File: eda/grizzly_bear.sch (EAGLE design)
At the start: 60 parts, among them Q1 N-CHANNEL-MOSFET, Q2 N-CHANNEL-MOSFET, Q3 N-CHANNEL-MOSFET, Q4 N-CHANNEL-MOSFET, Q5 IPD90P03P4L, U1 A4940, U2 ATMEGA32U4-AU, U3 ACS714, U4 UA78L00, U5 ISL83491SOIC, Y1 16MHz

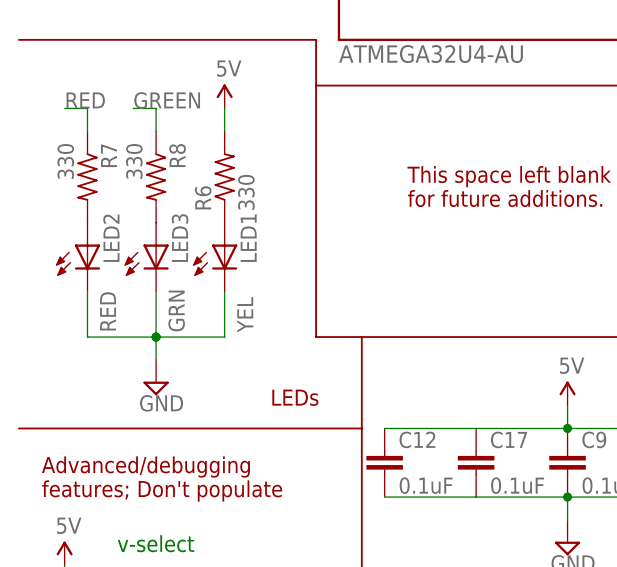
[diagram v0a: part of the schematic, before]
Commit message: Fix some LED BOM values
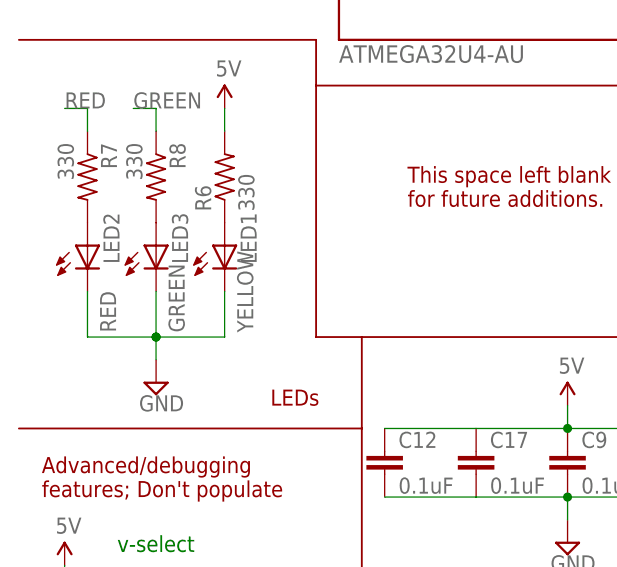
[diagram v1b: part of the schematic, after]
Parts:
- LED1: value YEL -> YELLOW
- LED3: value GRN -> GREEN
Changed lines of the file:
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@@
 <part name="C9" library="pie" deviceset="CAP" device="0603-CAP" value="0.1uF"/>
 <part name="LED2" library="pie" deviceset="LED" device="0805" value="RED"/>
-<part name="LED3" library="pie" deviceset="LED" device="0805" value="GRN"/>
+<part name="LED3" library="pie" deviceset="LED" device="0805" value="GREEN"/>
 <part name="R8" library="pie" deviceset="R-US_" device="R0603" value="330"/>
 <part name="R7" library="pie" deviceset="R-US_" device="R0603" value="330"/>
-<part name="LED1" library="pie" deviceset="LED" device="0805" value="YEL"/>
+<part name="LED1" library="pie" deviceset="LED" device="0805" value="YELLOW"/>
 <part name="R6" library="pie" deviceset="R-US_" device="R0603" value="330"/>
 <part name="U$13" library="pie" deviceset="5V" device=""/>

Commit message: Add even more BOM metadata
Only missing a small handful of parts
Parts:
- C8: value 470nF -> .47 uF
- Q1, Q2, Q3, Q4: value N-CHANNEL-MOSFET -> PSMN4R0
- SV2: device con-lstb:MA04-2 -> pie:MA04-2
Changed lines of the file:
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@@
 <part name="U$5" library="pie" deviceset="5V" device=""/>
 <part name="C16" library="pie" deviceset="CAP" device="0603-CAP" value="0.1uF"/>
-<part name="C8" library="pie" deviceset="CAP" device="0603-CAP" value="470nF"/>
+<part name="C8" library="pie" deviceset="CAP" device="0603-CAP" value=".47 uF"/>
 <part name="C6" library="pie" deviceset="CAP" device="0603-CAP" value="1uF"/>
 <part name="C7" library="pie" deviceset="CAP" device="0603-CAP" value="33nF"/>
@@
 <part name="Y1" library="pie" deviceset="CRYSTAL" device="SMD" value="16MHz"/>
 <part name="SV1" library="pie" deviceset="MA03-2" device=""/>
-<part name="Q1" library="pie" deviceset="N-CHANNEL-MOSFET" device=""/>
-<part name="Q2" library="pie" deviceset="N-CHANNEL-MOSFET" device=""/>
-<part name="Q3" library="pie" deviceset="N-CHANNEL-MOSFET" device=""/>
-<part name="Q4" library="pie" deviceset="N-CHANNEL-MOSFET" device=""/>
+<part name="Q1" library="pie" deviceset="N-CHANNEL-MOSFET" device="" value="PSMN4R0"/>
+<part name="Q2" library="pie" deviceset="N-CHANNEL-MOSFET" device="" value="PSMN4R0"/>
+<part name="Q3" library="pie" deviceset="N-CHANNEL-MOSFET" device="" value="PSMN4R0"/>
+<part name="Q4" library="pie" deviceset="N-CHANNEL-MOSFET" device="" value="PSMN4R0"/>
 <part name="Q5" library="pie" deviceset="P-CHANNEL-MOSFET" device="TO252" value="IPD90P03P4L"/>
 <part name="JP1" library="pie" deviceset="M02" device="PTH" value="GND"/>
@@
 <part name="SUPPLY9" library="pie" deviceset="GND" device=""/>
 <part name="U$15" library="pie" deviceset="5V" device=""/>
-<part name="SV2" library="con-lstb" deviceset="MA04-2" device=""/>
+<part name="SV2" library="pie" deviceset="MA04-2" device=""/>
 <part name="C17" library="pie" deviceset="CAP" device="0603-CAP" value="0.1uF"/>
 </parts>

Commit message: All BOM metadata for explicit parts added
Changed C4 on Grizzly to 1206 and moved around parts so that plane
is not interrupted as much.

Smartsensor filter permutations are not embedded in the BOM metadata
and will be documented elsewhere.
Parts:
- C4: device pie:CAP0603-CAP -> pie:CAP1206
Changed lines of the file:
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@@
 <grid distance="0.1" unitdist="inch" unit="inch" style="lines" multiple="1" display="yes" altdistance="0.05" altunitdist="inch" altunit="inch"/>
 <layers>
-<layer number="1" name="Top" color="4" fill="1" visible="no" active="no"/>
-<layer number="2" name="Route2" color="1" fill="3" visible="no" active="no"/>
-<layer number="3" name="Route3" color="4" fill="3" visible="no" active="no"/>
-<layer number="4" name="Route4" color="1" fill="4" visible="no" active="no"/>
-<layer number="5" name="Route5" color="4" fill="4" visible="no" active="no"/>
-<layer number="6" name="Route6" color="1" fill="8" visible="no" active="no"/>
-<layer number="7" name="Route7" color="4" fill="8" visible="no" active="no"/>
-<layer number="8" name="Route8" color="1" fill="2" visible="no" active="no"/>
-<layer number="9" name="Route9" color="4" fill="2" visible="no" active="no"/>
-<layer number="10" name="Route10" color="1" fill="7" visible="no" active="no"/>
-<layer number="11" name="Route11" color="4" fill="7" visible="no" active="no"/>
-<layer number="12" name="Route12" color="1" fill="5" visible="no" active="no"/>
-<layer number="13" name="Route13" color="4" fill="5" visible="no" active="no"/>
-<layer number="14" name="Route14" color="1" fill="6" visible="no" active="no"/>
-<layer number="15" name="Route15" color="4" fill="6" visible="no" active="no"/>
-<layer number="16" name="Bottom" color="1" fill="1" visible="no" active="no"/>
-<layer number="17" name="Pads" color="2" fill="1" visible="no" active="no"/>
-<layer number="18" name="Vias" color="2" fill="1" visible="no" active="no"/>
-<layer number="19" name="Unrouted" color="6" fill="1" visible="no" active="no"/>
-<layer number="20" name="Dimension" color="15" fill="1" visible="no" active="no"/>
-<layer number="21" name="tPlace" color="16" fill="1" visible="no" active="no"/>
-<layer number="22" name="bPlace" color="14" fill="1" visible="no" active="no"/>
-<layer number="23" name="tOrigins" color="15" fill="1" visible="no" active="no"/>
-<layer number="24" name="bOrigins" color="15" fill="1" visible="no" active="no"/>
-<layer number="25" name="tNames" color="7" fill="1" visible="no" active="no"/>
-<layer number="26" name="bNames" color="12" fill="1" visible="no" active="no"/>
-<layer number="27" name="tValues" color="7" fill="1" visible="no" active="no"/>
-<layer number="28" name="bValues" color="12" fill="1" visible="no" active="no"/>
+<layer number="1" name="Top" color="4" fill="1" visible="yes" active="no"/>
+<layer number="2" name="Route2" color="1" fill="3" visible="yes" active="no"/>
+<layer number="3" name="Route3" color="20" fill="3" visible="yes" active="no"/>
+<layer number="4" name="Route4" color="21" fill="4" visible="yes" active="no"/>
+<layer number="5" name="Route5" color="4" fill="4" visible="yes" active="no"/>
+<layer number="6" name="Route6" color="1" fill="8" visible="yes" active="no"/>
+<layer number="7" name="Route7" color="4" fill="8" visible="yes" active="no"/>
+<layer number="8" name="Route8" color="1" fill="2" visible="yes" active="no"/>
+<layer number="9" name="Route9" color="4" fill="2" visible="yes" active="no"/>
+<layer number="10" name="Route10" color="1" fill="7" visible="yes" active="no"/>
+<layer number="11" name="Route11" color="4" fill="7" visible="yes" active="no"/>
+<layer number="12" name="Route12" color="1" fill="5" visible="yes" active="no"/>
+<layer number="13" name="Route13" color="4" fill="5" visible="yes" active="no"/>
+<layer number="14" name="Route14" color="1" fill="6" visible="yes" active="no"/>
+<layer number="15" name="Route15" color="4" fill="6" visible="yes" active="no"/>
+<layer number="16" name="Bottom" color="1" fill="1" visible="yes" active="no"/>
+<layer number="17" name="Pads" color="2" fill="1" visible="yes" active="no"/>
+<layer number="18" name="Vias" color="2" fill="1" visible="yes" active="no"/>
+<layer number="19" name="Unrouted" color="6" fill="1" visible="yes" active="no"/>
+<layer number="20" name="Dimension" color="15" fill="1" visible="yes" active="no"/>
+<layer number="21" name="tPlace" color="16" fill="1" visible="yes" active="no"/>
+<layer number="22" name="bPlace" color="17" fill="1" visible="yes" active="no"/>
+<layer number="23" name="tOrigins" color="15" fill="1" visible="yes" active="no"/>
+<layer number="24" name="bOrigins" color="15" fill="1" visible="yes" active="no"/>
+<layer number="25" name="tNames" color="18" fill="1" visible="yes" active="no"/>
+<layer number="26" name="bNames" color="19" fill="1" visible="yes" active="no"/>
+<layer number="27" name="tValues" color="18" fill="1" visible="yes" active="no"/>
+<layer number="28" name="bValues" color="19" fill="1" visible="yes" active="no"/>
 <layer number="29" name="tStop" color="7" fill="3" visible="no" active="no"/>
 <layer number="30" name="bStop" color="7" fill="6" visible="no" active="no"/>
@@
 <layer number="35" name="tGlue" color="7" fill="4" visible="no" active="no"/>
 <layer number="36" name="bGlue" color="7" fill="5" visible="no" active="no"/>
-<layer number="37" name="tTest" color="7" fill="1" visible="no" active="no"/>
-<layer number="38" name="bTest" color="7" fill="1" visible="no" active="no"/>
+<layer number="37" name="tTest" color="7" fill="1" visible="yes" active="no"/>
+<layer number="38" name="bTest" color="7" fill="1" visible="yes" active="no"/>
 <layer number="39" name="tKeepout" color="4" fill="11" visible="no" active="no"/>
 <layer number="40" name="bKeepout" color="1" fill="11" visible="no" active="no"/>
@@
 <layer number="44" name="Drills" color="7" fill="1" visible="no" active="no"/>
 <layer number="45" name="Holes" color="7" fill="1" visible="no" active="no"/>
-<layer number="46" name="Milling" color="3" fill="1" visible="no" active="no"/>
-<layer number="47" name="Measures" color="7" fill="1" visible="no" active="no"/>
-<layer number="48" name="Document" color="7" fill="1" visible="no" active="no"/>
-<layer number="49" name="Reference" color="7" fill="1" visible="no" active="no"/>
-<layer number="50" name="dxf" color="7" fill="1" visible="no" active="no"/>
-<layer number="51" name="tDocu" color="6" fill="1" visible="no" active="no"/>
-<layer number="52" name="bDocu" color="7" fill="1" visible="no" active="no"/>
-<layer number="53" name="tGND_GNDA" color="7" fill="9" visible="no" active="no"/>
-<layer number="54" name="bGND_GNDA" color="1" fill="9" visible="no" active="no"/>
-<layer number="56" name="wert" color="7" fill="1" visible="no" active="no"/>
+<layer number="46" name="Milling" color="3" fill="1" visible="yes" active="no"/>
+<layer number="47" name="Measures" color="7" fill="1" visible="yes" active="no"/>
+<layer number="48" name="Document" color="7" fill="1" visible="yes" active="no"/>
+<layer number="49" name="Reference" color="7" fill="1" visible="yes" active="no"/>
+<layer number="50" name="dxf" color="7" fill="1" visible="yes" active="no"/>
+<layer number="51" name="tDocu" color="6" fill="1" visible="yes" active="no"/>
+<layer number="52" name="bDocu" color="6" fill="1" visible="yes" active="no"/>
+<layer number="53" name="tGND_GNDA" color="7" fill="9" visible="yes" active="no"/>
+<layer number="54" name="bGND_GNDA" color="1" fill="9" visible="yes" active="no"/>
+<layer number="56" name="wert" color="7" fill="1" visible="yes" active="no"/>
 <layer number="91" name="Nets" color="2" fill="1" visible="yes" active="yes"/>
 <layer number="92" name="Busses" color="1" fill="1" visible="yes" active="yes"/>
@@
 <part name="R11" library="pie" deviceset="R-US_" device="R0603" value="10k"/>
 <part name="SUPPLY17" library="pie" deviceset="GND" device=""/>
-<part name="C4" library="pie" deviceset="CAP" device="0603-CAP" value="10uF"/>
+<part name="C4" library="pie" deviceset="CAP" device="1206" value="10uF"/>
 <part name="R1" library="pie" deviceset="R-US_" device="R0603" value="10k"/>
 <part name="U$2" library="pie" deviceset="USB-M26FTR" device=""/>
